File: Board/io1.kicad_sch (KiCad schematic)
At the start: 1 part, among them U1 XC6SLX9-TQG144

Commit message: update
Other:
- moved on the sheet: U1B

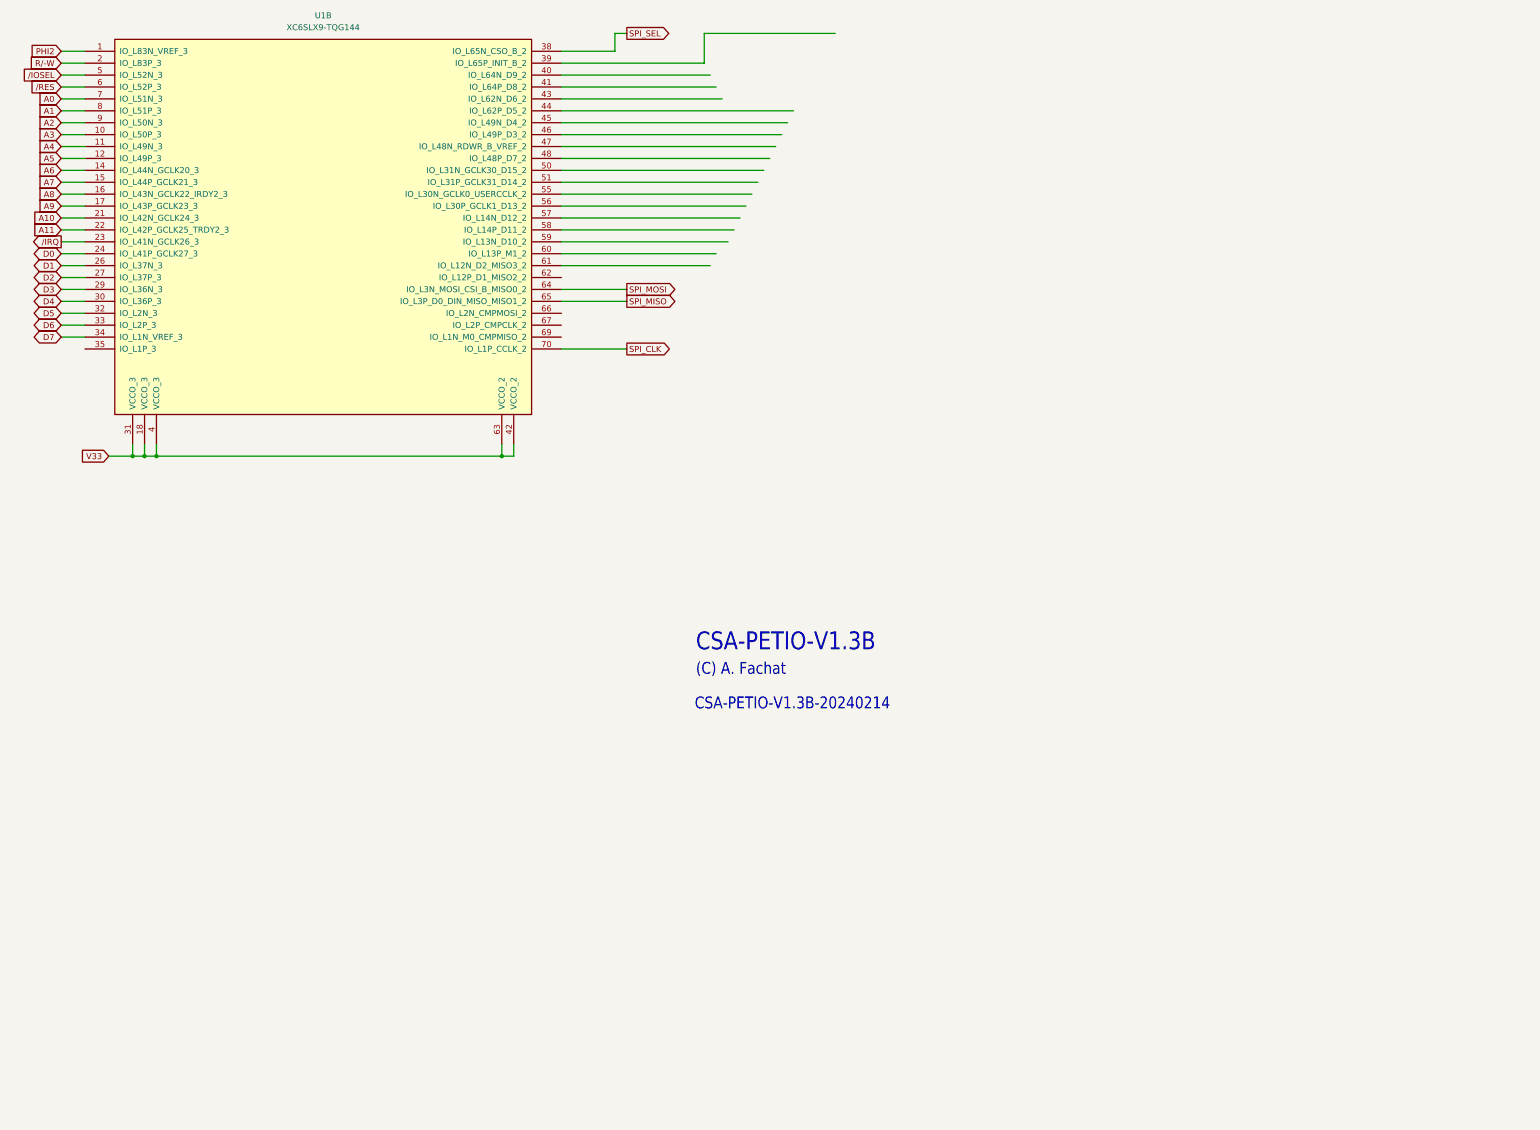
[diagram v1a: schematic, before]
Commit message: add serial, SPI-10-5V
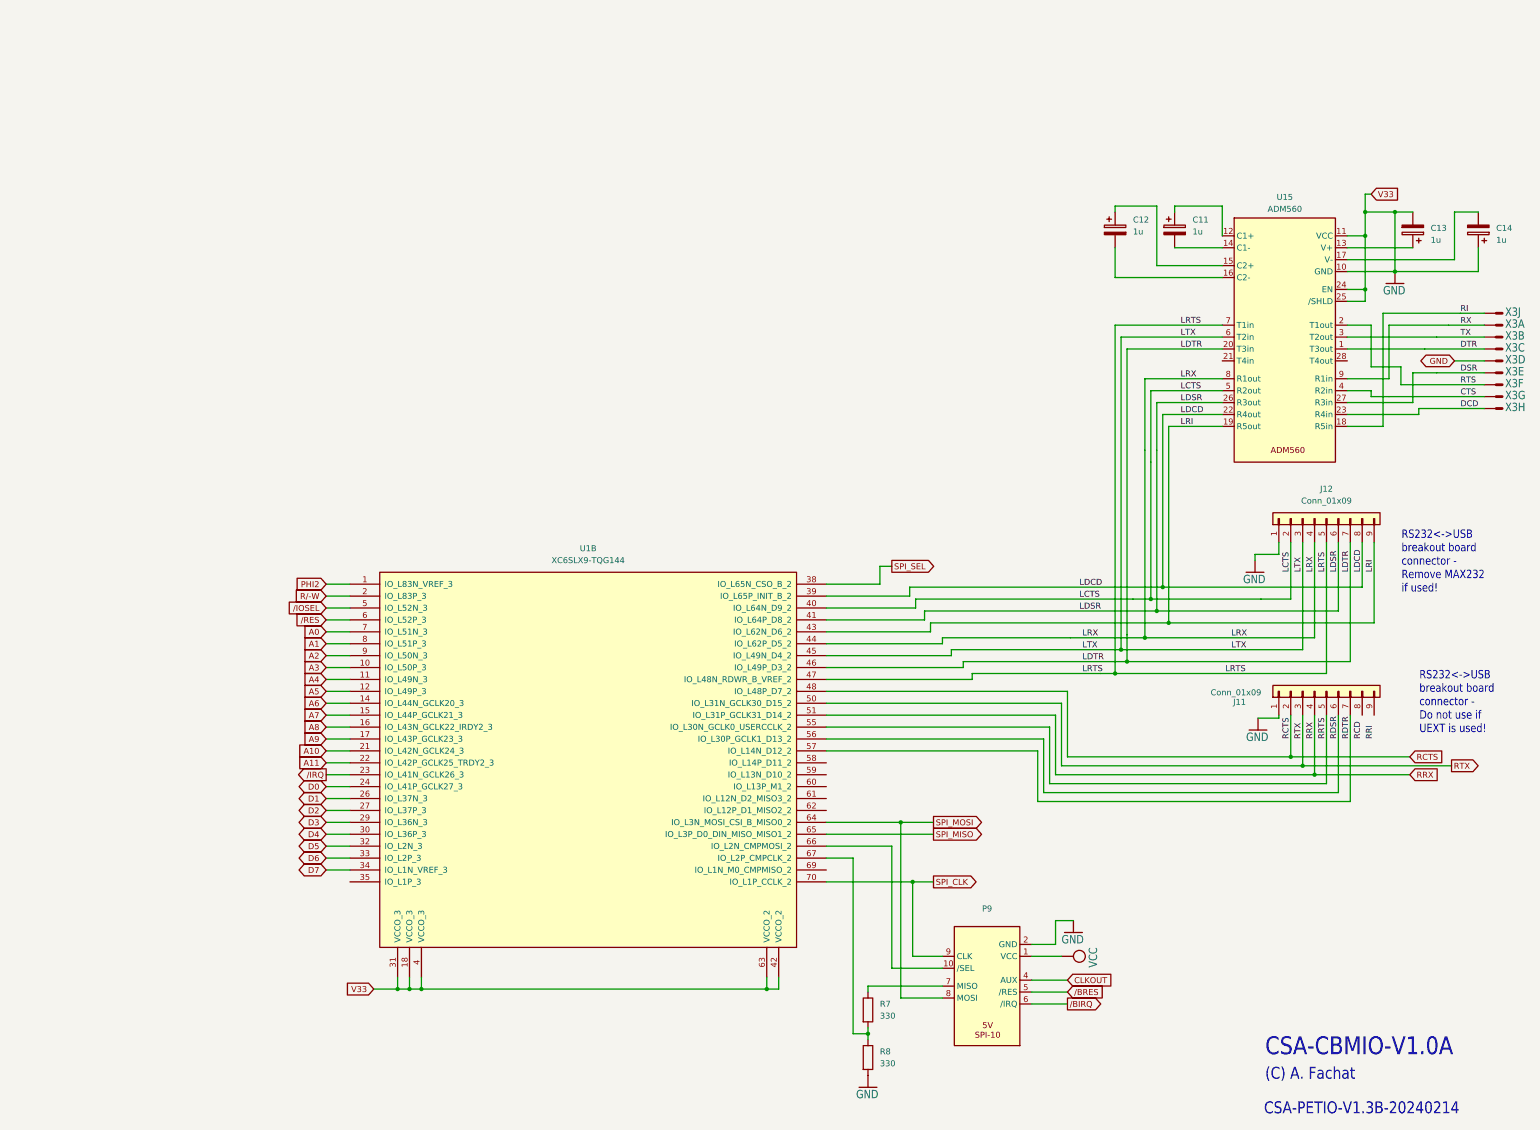
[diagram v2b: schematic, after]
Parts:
- added C11, C12, C13, C14: 1u, Capacitor_SMD:C_0805_2012Metric_Pad1.18x1.45mm_HandSolder, symbol Device:C_Polarized
- added J11, J12: Conn_01x09, Connector_PinHeader_2.54mm:PinHeader_1x09_P2.54mm_Vertical, symbol Connector_Generic:Conn_01x09
- added P9: ~, Connector_IDC:IDC-Header_2x05_P2.54mm_Vertical, symbol SPI:SPI-10-5V
- added R7, R8: 330, Resistor_SMD:R_0603_1608Metric_Pad0.98x0.95mm_HandSolder, symbol Device:R
- added U15: ADM560, Package_SO:SSOP-28_5.3x10.2mm_P0.65mm, symbol csa_petio_v1-eagle-import:ADM560
- added X3: M09HPS, Connector_Dsub:DSUB-9_Pins_Horizontal_P2.77x2.84mm_EdgePinOffset9.90mm_Housed_MountingHolesOffset11.32mm, symbol cbm_ultipet_v1-eagle-import:M09HPS
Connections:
- net SPI_CLK: now also P9.9 (CLK)
- net SPI_MOSI: now also P9.8 (MOSI)
- net LDCD: now reaches U1.39 (IO_L65P_INIT_B_2)
- net LDCD: now also J12.8 (Pin_8), U15.22 (R4out)
- net LCTS: now reaches U1.40 (IO_L64N_D9_2)
- net LCTS: now also J12.2 (Pin_2), U15.5 (R2out)
- net LDSR: now reaches U1.41 (IO_L64P_D8_2)
- net LDSR: now also J12.6 (Pin_6), U15.26 (R3out)
- net LRI: now reaches U1.43 (IO_L62N_D6_2)
- net LRI: now also J12.9 (Pin_9), U15.19 (R5out)
- net LRX: now reaches U1.44 (IO_L62P_D5_2)
- net LRX: now also J12.4 (Pin_4), U15.8 (R1out)
- net LTX: now reaches U1.45 (IO_L49N_D4_2)
- net LTX: now also J12.3 (Pin_3), U15.6 (T2in)
- net LDTR: now reaches U1.46 (IO_L49P_D3_2)
- net LDTR: now also J12.7 (Pin_7), U15.20 (T3in)
- net LRTS: now reaches U1.47 (IO_L48N_RDWR_B_VREF_2)
- net LRTS: now also J12.5 (Pin_5), U15.7 (T1in)
- net RCTS: now reaches U1.48 (IO_L48P_D7_2)
- net RCTS: now also J11.2 (Pin_2)
- net RTX: now reaches U1.50 (IO_L31N_GCLK30_D15_2)
- net RTX: now also J11.3 (Pin_3)
- net RRX: now reaches U1.51 (IO_L31P_GCLK31_D14_2)
- net RRX: now also J11.4 (Pin_4)
- net RRTS: now reaches U1.55 (IO_L30N_GCLK0_USERCCLK_2)
- net RRTS: now also J11.5 (Pin_5)
- net RDSR: now reaches U1.56 (IO_L30P_GCLK1_D13_2)
- net RDSR: now also J11.6 (Pin_6)
- net RDTR: now reaches U1.57 (IO_L14N_D12_2)
- net RDTR: now also J11.7 (Pin_7)
- net at U1.66 (IO_L2N_CMPMOSI_2): now also P9.10 (/SEL)
- net at U1.67 (IO_L2P_CMPCLK_2): now also R7.2, R8.1
- net V33 renamed GND
- net GND: now also C13.2, C14.1, J11.1 (Pin_1), J12.1 (Pin_1), P9.2 (GND), R8.2, U15.10 (GND), U15.11 (VCC), U15.24 (EN), U15.25 (/SHLD), X3.5 (M)
- new net: C11.1, U15.12 (C1+)
- new net: C13.1, U15.13 (V+)
- new net: C11.2, U15.14 (C1-)
- new net: C12.1, U15.15 (C2+)
- new net: C12.2, U15.16 (C2-)
- new net: C14.2, U15.17 (V-)
- new net: P9.7 (MISO), R7.1
- new net CLKOUT: P9.4 (AUX)
- new net CTS: U15.4 (R2in), X3.8 (M)
- new net DCD: U15.23 (R4in), X3.9 (M)
- new net DSR: U15.27 (R3in), X3.6 (M)
- new net DTR: U15.1 (T3out), X3.4 (M)
- new net RI: U15.18 (R5in), X3.1 (M)
- new net RTS: U15.2 (T1out), X3.7 (M)
- new net RX: U15.9 (R1in), X3.2 (M)
- new net TX: U15.3 (T2out), X3.3 (M)
- new net VCC: P9.1 (VCC)
- new net /BIRQ: P9.6 (/IRQ)
- new net /BRES: P9.5 (/RES)
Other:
- note added: "CSA-CBMIO-V1.0A"
- note added: "RS232<->USB breakout board connector - Do not use if UEXT is used!"
- note added: "RS232<->USB breakout board connector - Remove MAX232 if used!"
- note removed: "CSA-PETIO-V1.3B"
- moved on the sheet: U1B

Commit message: schematics 1st full rev
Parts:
- added P5: CBMTAPE, csa_petio_v1:JP6, symbol csa_petio_v1-eagle-import:CBMTAPE
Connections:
- net GND: now also P5.1 (GND)
- net VCC: now also P5.2 (VCC)
- net /BE: now reaches U1.35 (IO_L1P_3)
- net C1SW: now reaches U1.58 (IO_L14P_D11_2)
- net C1SW: now also P5.6 (SWITCH)
- net C1RD: now reaches U1.59 (IO_L13N_D10_2)
- net C1RD: now also P5.4 (READ)
- net CWR: now reaches U1.60 (IO_L13P_M1_2)
- net CWR: now also P5.5 (WRITE)
- net C1MTR: now reaches U1.61 (IO_L12N_D2_MISO3_2)
- net C1MTR: now also P5.3 (MOTOR)
- net UP12: now reaches U1.62 (IO_L12P_D1_MISO2_2)
- net UP13: now reaches U1.69 (IO_L1N_M0_CMPMISO_2)
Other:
- note added: "CSA-CBMIO-V1.0A-20250815"
- note removed: "CSA-PETIO-V1.3B-20240214"
- moved on the sheet: C11, C12, C13, C14, J11, J12, P9, R7, R8, U15, U1B, X3A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

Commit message: full connect, starting on prod
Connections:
- net GND: no longer C13.2, U1.18 (VCCO_3), U1.31 (VCCO_3), U1.4 (VCCO_3), U1.42 (VCCO_2), U1.63 (VCCO_2), U15.11 (VCC), U15.24 (EN), U15.25 (/SHLD)
- net LCTS: now also U1.39 (IO_L65P_INIT_B_2); no longer U1.40 (IO_L64N_D9_2)
- net LDCD: now also U1.46 (IO_L49P_D3_2); no longer U1.39 (IO_L65P_INIT_B_2)
- net LDSR: now also U1.44 (IO_L62P_D5_2); no longer U1.41 (IO_L64P_D8_2)
- net LDTR: now also U1.45 (IO_L49N_D4_2); no longer U1.46 (IO_L49P_D3_2)
- net LRI: now also U1.47 (IO_L48N_RDWR_B_VREF_2); no longer U1.43 (IO_L62N_D6_2)
- net LRTS: now also U1.43 (IO_L62N_D6_2); no longer U1.47 (IO_L48N_RDWR_B_VREF_2)
- net LRX: now also U1.41 (IO_L64P_D8_2); no longer U1.44 (IO_L62P_D5_2)
- net LTX: now also U1.40 (IO_L64N_D9_2); no longer U1.45 (IO_L49N_D4_2)
- new net V33: C13.2, U1.18 (VCCO_3), U1.31 (VCCO_3), U1.4 (VCCO_3), U1.42 (VCCO_2), U1.63 (VCCO_2), U15.11 (VCC), U15.24 (EN), U15.25 (/SHLD)
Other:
- moved on the sheet: U1B

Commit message: 1st working as 1.0B
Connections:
- net PHI2: now also U1.23 (IO_L41N_GCLK26_3); no longer U1.1 (IO_L83N_VREF_3)
- net /IRQ: now also U1.1 (IO_L83N_VREF_3); no longer U1.23 (IO_L41N_GCLK26_3)
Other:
- note added: "1.0B: swap /IRQ and PHI2, so PHI2 gets a GCLK pin"
- note added: "CSA-CBMIO-V1.0B"
- note added: "CSA-CBMIO-V1.0B-20260321"
- note removed: "CSA-CBMIO-V1.0A"
- note removed: "CSA-CBMIO-V1.0A-20250815"
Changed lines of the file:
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@@
 	(generator_version "9.0")
 	(paper "A3")
-	(text "CSA-CBMIO-V1.0A-20250815"
+	(text "1.0B: swap /IRQ and PHI2, so PHI2 gets a GCLK pin"
+		(exclude_from_sim no)
+		(at 344.17 244.094 0)
+		(effects
+			(font
+				(size 2.54 2.54)
+			)
+		)
+	)
+	(text "CSA-CBMIO-V1.0B-20260321"
 		(exclude_from_sim no)
 		(at 332.232 273.304 0)
@@
 		)
 	)
-	(text "CSA-CBMIO-V1.0A"
+	(text "CSA-CBMIO-V1.0B"
 		(exclude_from_sim no)
 		(at 331.47 261.112 0)
@@
 	(wire
 		(pts
-			(xy 86.36 160.02) (xy 91.44 160.02)
-		)
-		(stroke
-			(width 0)
-			(type default)
-		)
-	)
-	(wire
-		(pts
 			(xy 213.36 129.54) (xy 213.36 132.08)
 		)
@@
 	(wire
 		(pts
+			(xy 86.36 160.02) (xy 91.44 160.02)
+		)
+		(stroke
+			(width 0)
+			(type default)
+		)
+	)
+	(wire
+		(pts
 			(xy 158.75 228.6) (xy 180.34 228.6)
 		)
@@
 	(wire
 		(pts
+			(xy 85.725 119.38) (xy 91.44 119.38)
+		)
+		(stroke
+			(width 0)
+			(type default)
+		)
+	)
+	(wire
+		(pts
 			(xy 158.75 238.76) (xy 163.83 238.76)
 		)
@@
 	(wire
 		(pts
-			(xy 86.36 119.38) (xy 91.44 119.38)
-		)
-		(stroke
-			(width 0)
-			(type default)
-		)
-	)
-	(wire
-		(pts
 			(xy 262.89 38.1) (xy 254 38.1)
 		)
@@
 	(global_label "{slash}IRQ"
 		(shape output)
-		(at 86.36 160.02 180)
+		(at 85.725 119.38 180)
 		(fields_autoplaced yes)
 		(effects
@@
 		)
 		(property "Intersheetrefs" "${INTERSHEET_REFS}"
-			(at 78.839 160.02 0)
+			(at 78.204 119.38 0)
 			(effects
 				(font
@@
 	(global_label "PHI2"
 		(shape input)
-		(at 86.36 119.38 180)
+		(at 86.36 160.02 180)
 		(fields_autoplaced yes)
 		(effects
@@
 		)
 		(property "Intersheetrefs" "${INTERSHEET_REFS}"
-			(at 78.96 119.38 0)
+			(at 78.96 160.02 0)
 			(effects
 				(font
